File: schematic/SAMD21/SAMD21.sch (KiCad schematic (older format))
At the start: 1 part, among them IC1 ATSAMD21G18A-AU

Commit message: Complete schematic
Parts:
- IC1: footprint QFP50P900X900X120-48N -> SamacSys_Parts:QFP50P900X900X120-48N
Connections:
- net PA08: now reaches IC1.13 (PA08)
- net PA09: now reaches IC1.14 (PA09)
- net PA10: now reaches IC1.15 (PA10)
- net PA11: now reaches IC1.16 (PA11)
- net PB10: now reaches IC1.19 (PB10)
- net PB11: now reaches IC1.20 (PB11)
- net PA12: now reaches IC1.21 (PA12)
- net PA13: now reaches IC1.22 (PA13)
- net PA14: now reaches IC1.23 (PA14)
- net PA15: now reaches IC1.24 (PA15)
- net PA18: now reaches IC1.27 (PA18)
- net PA19: now reaches IC1.28 (PA19)
- net PA20: now reaches IC1.29 (PA20)
- net PA21: now reaches IC1.30 (PA21)
- net PA22: now reaches IC1.31 (PA22)
- net VDDCORE: now reaches IC1.43 (VDDCORE)
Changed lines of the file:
@@
 F 0 "IC1" H 5350 2700 50  0000 L CNN
 F 1 "ATSAMD21G18A-AU" H 5100 1850 50  0000 L CNN
-F 2 "QFP50P900X900X120-48N" H 6150 3700 50  0001 L CNN
+F 2 "SamacSys_Parts:QFP50P900X900X120-48N" H 6150 3700 50  0001 L CNN
 F 3 "" H 6150 3600 50  0001 L CNN
 F 4 "ATMEL - ATSAMD21G18A-AU - MCU, 32BIT, CORTEX-M0+, 48MHZ, TQFP-48" H 6150 3500 50  0001 L CNN "Description"
@@
 Wire Wire Line
 	4300 4200 4600 4200
+Text GLabel 4900 5350 3    50   Input ~ 0
+PA08
+Text GLabel 5000 5350 3    50   Input ~ 0
+PA09
+Text GLabel 5100 5350 3    50   Input ~ 0
+PA10
+Text GLabel 5200 5350 3    50   Input ~ 0
+PA11
+Text GLabel 5500 5350 3    50   Input ~ 0
+PB10
+Text GLabel 5600 5350 3    50   Input ~ 0
+PB11
+Text GLabel 5700 5350 3    50   Input ~ 0
+PA12
+Text GLabel 5800 5350 3    50   Input ~ 0
+PA13
+Text GLabel 5900 5350 3    50   Input ~ 0
+PA14
+Text GLabel 6000 5350 3    50   Input ~ 0
+PA15
+Text GLabel 6700 4000 2    50   Input ~ 0
+PA18
+Text GLabel 6700 3900 2    50   Input ~ 0
+PA19
+Text GLabel 6700 3800 2    50   Input ~ 0
+PA20
+Text GLabel 6700 3700 2    50   Input ~ 0
+PA21
+Text GLabel 6700 3600 2    50   Input ~ 0
+PA22
+Wire Wire Line
+	6300 3600 6700 3600
+Wire Wire Line
+	6300 3700 6700 3700
+Wire Wire Line
+	6300 3800 6700 3800
+Wire Wire Line
+	6300 3900 6700 3900
+Wire Wire Line
+	6300 4000 6700 4000
+Wire Wire Line
+	4900 5000 4900 5350
+Wire Wire Line
+	5000 5000 5000 5350
+Wire Wire Line
+	5100 5000 5100 5350
+Wire Wire Line
+	5200 5000 5200 5350
+Wire Wire Line
+	5500 5000 5500 5350
+Wire Wire Line
+	5600 5000 5600 5350
+Wire Wire Line
+	5700 5000 5700 5350
+Wire Wire Line
+	5800 5000 5800 5350
+Wire Wire Line
+	5900 5000 5900 5350
+Wire Wire Line
+	6000 5000 6000 5350
+Text GLabel 5400 2200 1    50   Input ~ 0
+VDDCORE
+Wire Wire Line
+	5400 2300 5400 2200
 $EndSCHEMATC

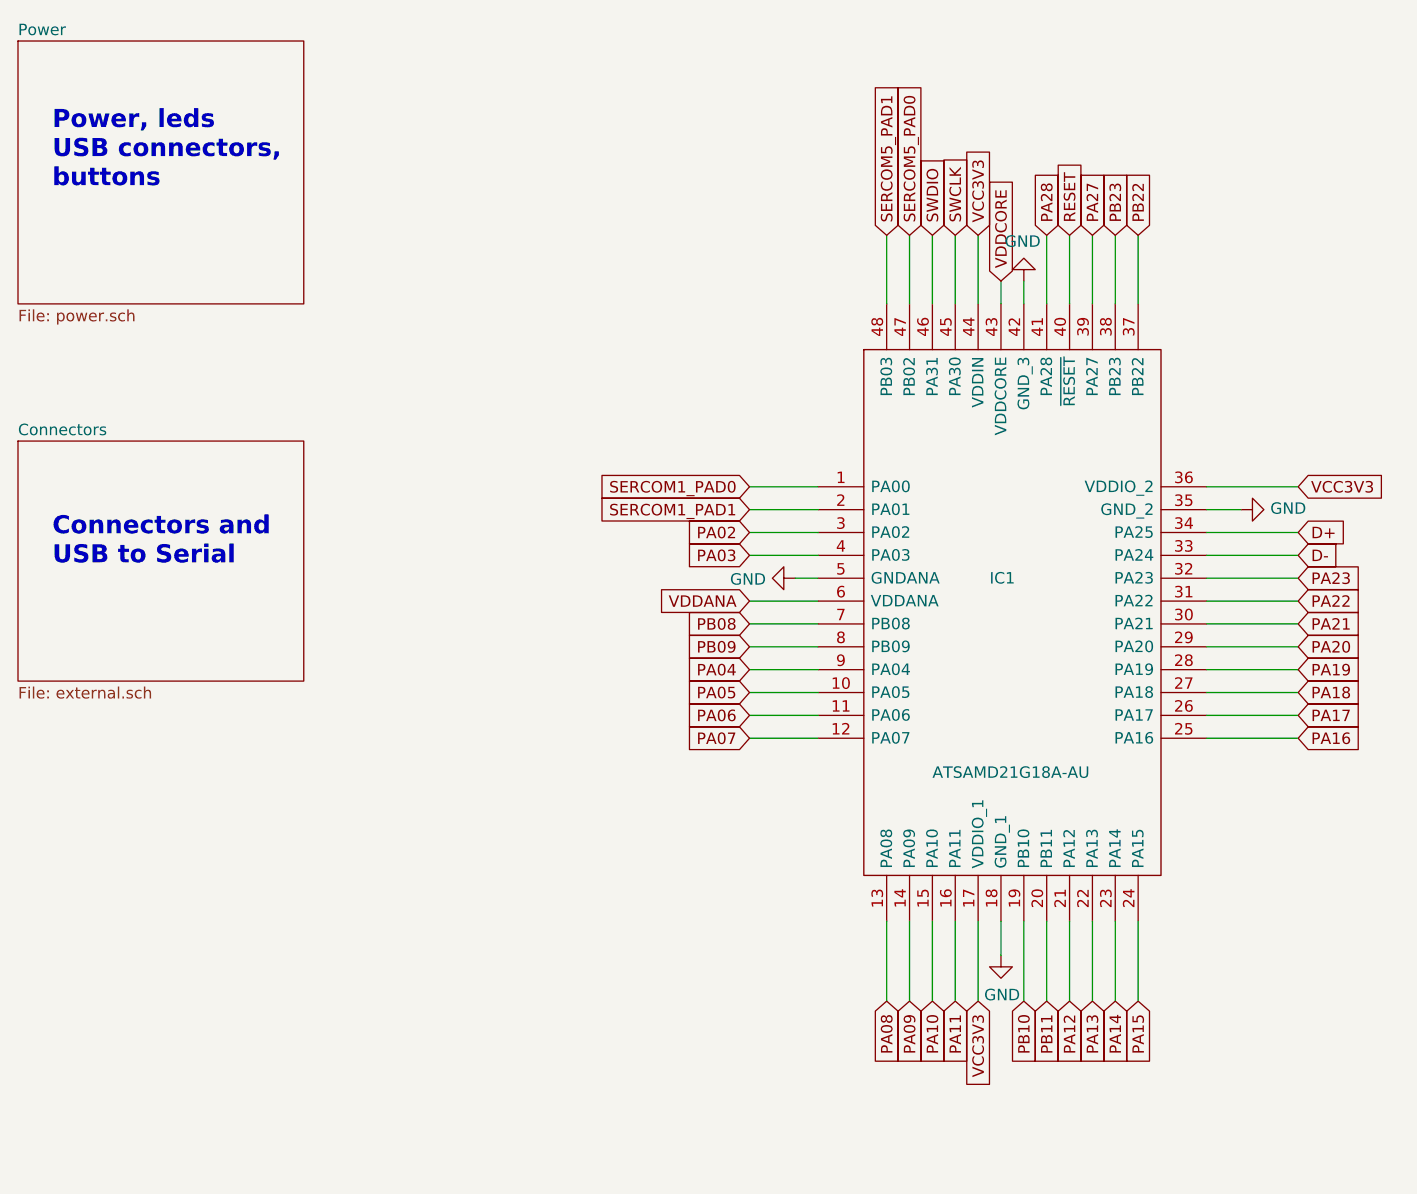
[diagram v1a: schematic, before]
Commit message: Moved I2C to pins with support for I2C
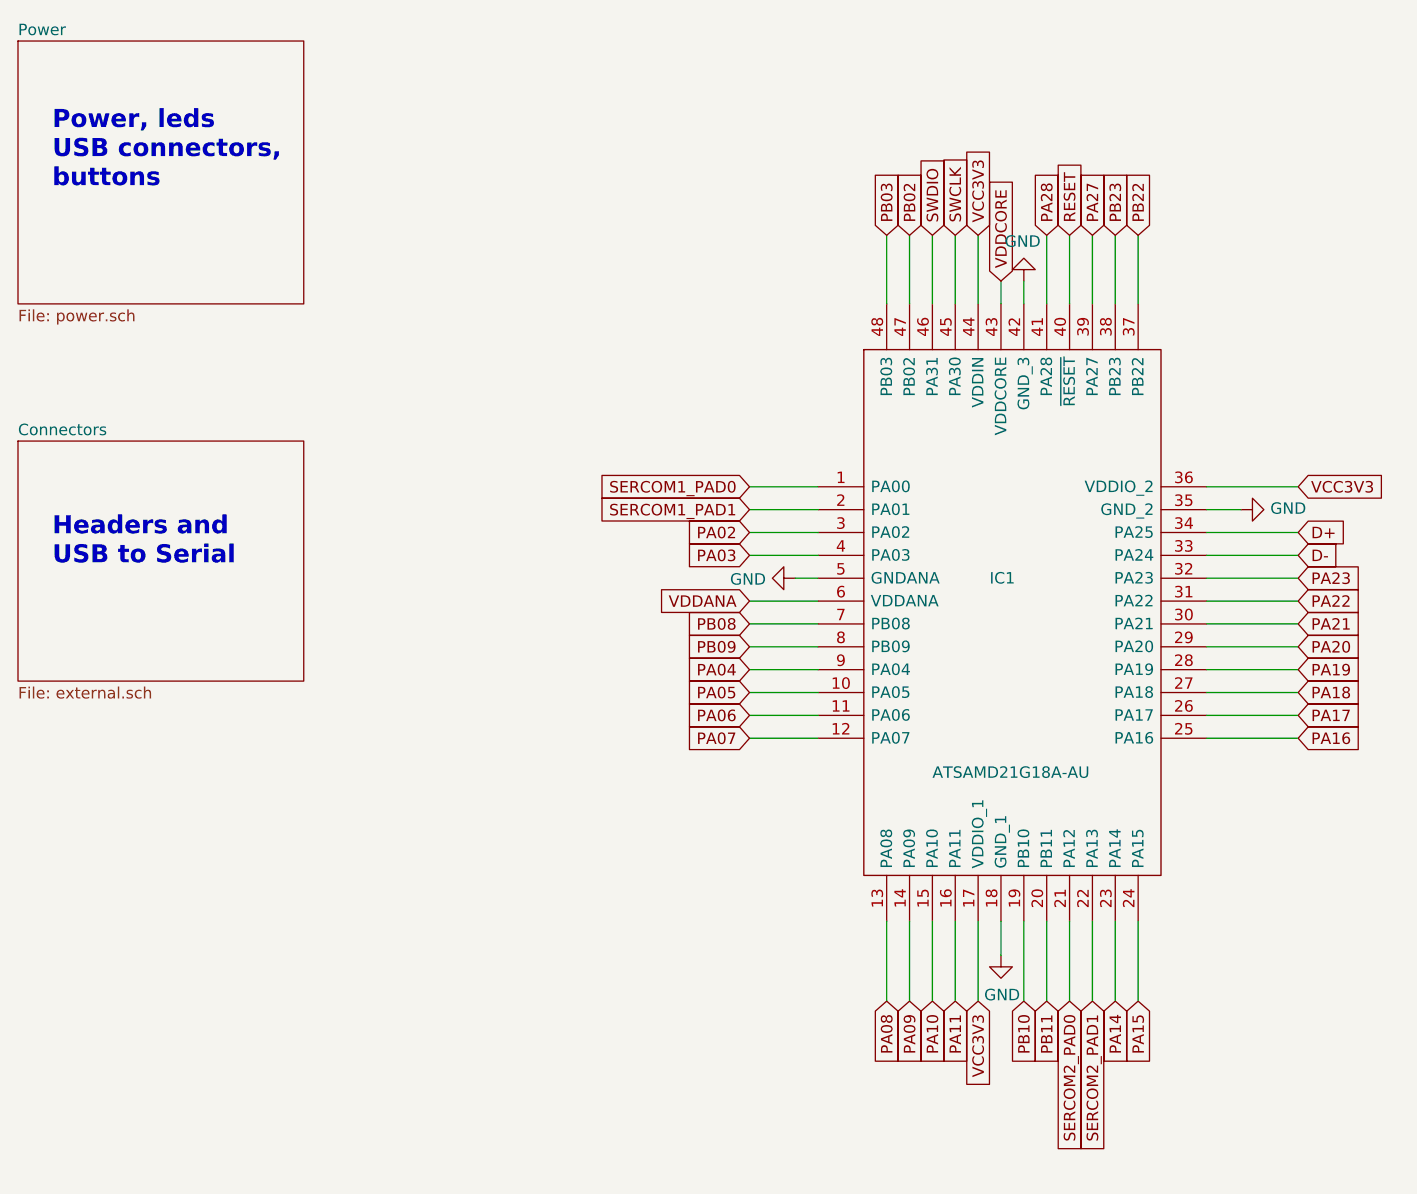
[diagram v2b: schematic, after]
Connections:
- net PA12 renamed SERCOM2_PAD0
- net PA13 renamed SERCOM2_PAD1
- net SERCOM5_PAD0 renamed PB02
- net SERCOM5_PAD1 renamed PB03
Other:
- note added: "Headers and\nUSB to Serial"
- note removed: "Connectors and\nUSB to Serial"
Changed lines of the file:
@@
 Power, leds\nUSB connectors,\nbuttons
 Text Notes 1250 3450 0    79   ~ 16
-Connectors and\nUSB to Serial
+Headers and\nUSB to Serial
 Text GLabel 5700 2000 1    50   Input ~ 0
 RESET
@@
 Text GLabel 4300 3200 0    50   Input ~ 0
 SERCOM1_PAD1
-Text GLabel 4900 2000 1    50   Input ~ 0
-SERCOM5_PAD1
-Text GLabel 5000 2000 1    50   Input ~ 0
-SERCOM5_PAD0
+Text GLabel 5800 5350 3    50   Input ~ 0
+SERCOM2_PAD1
+Text GLabel 5700 5350 3    50   Input ~ 0
+SERCOM2_PAD0
 Wire Wire Line
 	4600 3100 4300 3100
@@
 Text GLabel 5600 5350 3    50   Input ~ 0
 PB11
-Text GLabel 5700 5350 3    50   Input ~ 0
-PA12
-Text GLabel 5800 5350 3    50   Input ~ 0
-PA13
 Text GLabel 5900 5350 3    50   Input ~ 0
 PA14
@@
 Wire Wire Line
 	5400 2300 5400 2200
+Text GLabel 4900 2000 1    50   Input ~ 0
+PB03
+Text GLabel 5000 2000 1    50   Input ~ 0
+PB02
 $EndSCHEMATC

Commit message: minor fix
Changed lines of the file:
@@
 Wire Wire Line
 	6000 5000 6000 5350
-Text GLabel 5400 2200 1    50   Input ~ 0
+Text GLabel 5400 2000 1    50   Input ~ 0
 VDDCORE
-Wire Wire Line
-	5400 2300 5400 2200
 Text GLabel 4900 2000 1    50   Input ~ 0
 PB03
 Text GLabel 5000 2000 1    50   Input ~ 0
 PB02
+Wire Wire Line
+	5400 2000 5400 2300
 $EndSCHEMATC
